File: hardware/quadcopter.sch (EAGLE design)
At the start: 62 parts, among them J1 AVR_SPI_PRG_6NS, J2 HEADER-4POS-2X2-0.1IN-FEMALE-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, J3 HEADER-10POSTH-254X10, J4 HEADER-4POS-0.1IN-FEMALE-SMD-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, Q1 MOSFET-SI2302CDS-T1-E3CT-ND, Q2 MOSFET-SI2302CDS-T1-E3CT-ND, Q3 MOSFET-SI2302CDS-T1-E3CT-ND, Q4 MOSFET-SI2302CDS-T1-E3CT-ND, Q5 MOSFET-SI2302CDS-T1-E3CT-ND, Q6 MOSFET-SI2302CDS-T1-E3CT-ND, SW1 PUSHBUTTON_SMD-VERTICAL-1, U1 ATMEGA128RFA1, U2 LSM-IMU-497-18367-1-NDIMU, Y1 CRYSTAL5X3

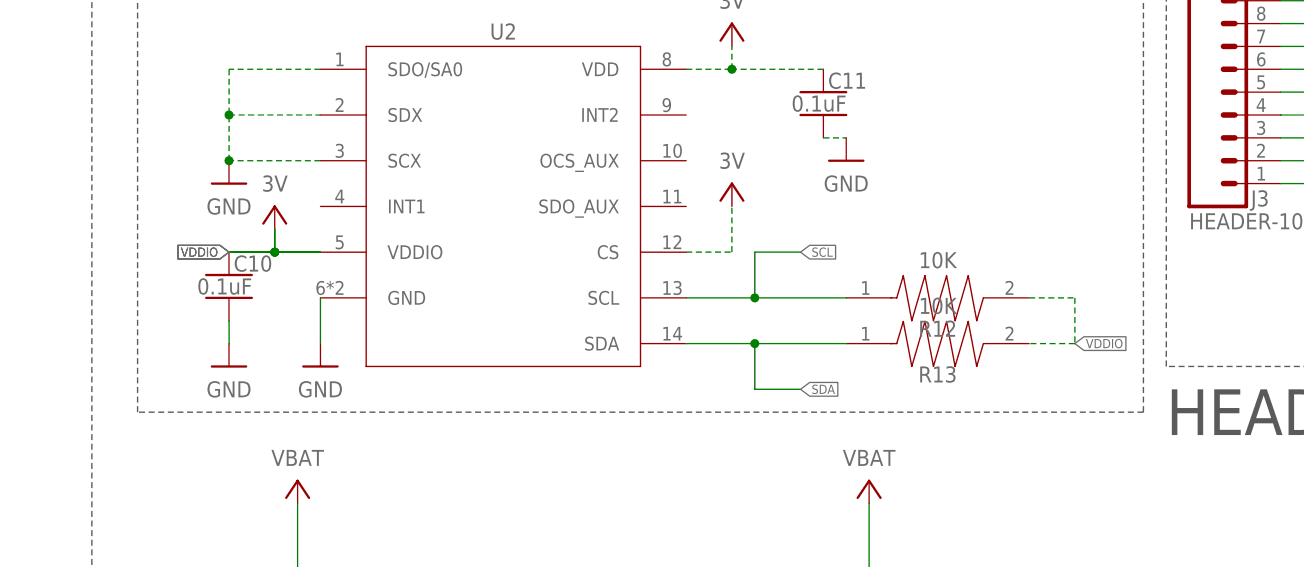
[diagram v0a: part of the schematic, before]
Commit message: switched pull up on SCL and SDA from 'VDDIO' to 3V
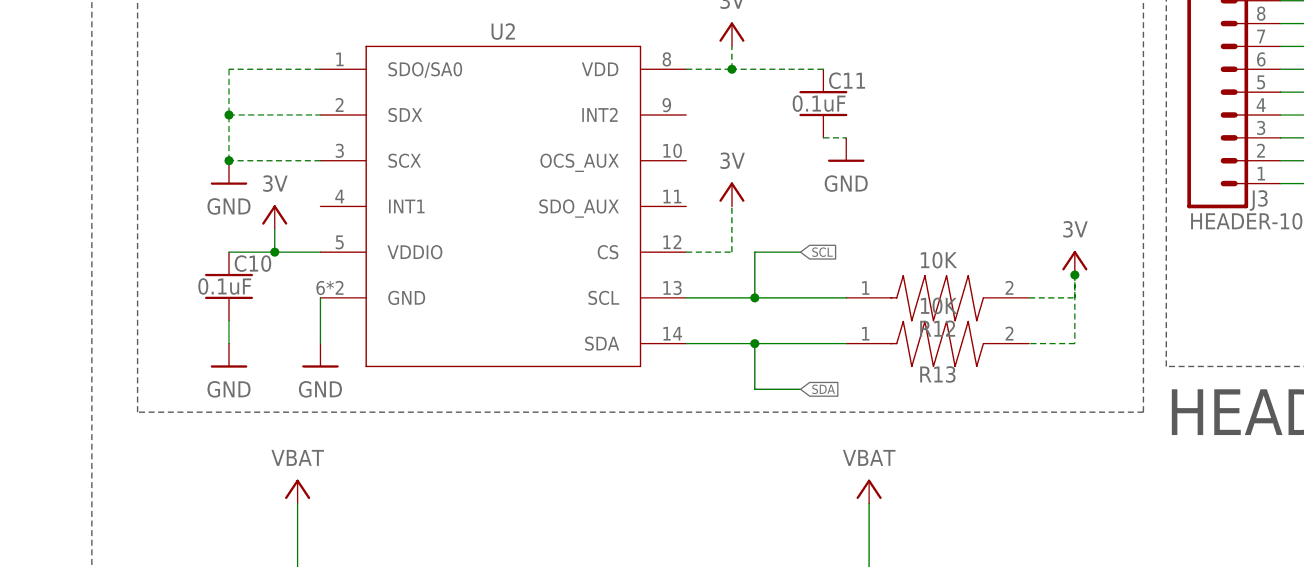
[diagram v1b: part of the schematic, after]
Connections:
- net 3V: now also R12.2, R13.2
- net VDDIO: no longer R12.2, R13.2
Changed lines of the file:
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@@
 <part name="GND4" library="quadparts_prebuilt_2022" deviceset="GND" device=""/>
 <part name="B2" library="quadparts_prebuilt_2022" deviceset="BATTERY" device="-SCREW-TERMINAL"/>
+<part name="P+21" library="quadparts_prebuilt_2022" deviceset="3V" device=""/>
 </parts>
 <sheets>
@@
 <attribute name="NAME" x="242.57" y="45.72" size="1.778" layer="95" font="vector" align="center"/>
 </instance>
+<instance part="P+21" gate="G$1" x="325.12" y="152.4" smashed="yes">
+<attribute name="VALUE" x="325.12" y="154.94" size="1.778" layer="96" rot="R180" align="center"/>
+</instance>
 </instances>
 <busses>
@@
 <pinref part="J3" gate="G$1" pin="10"/>
 </segment>
+<segment>
+<wire x1="320.04" y1="147.32" x2="325.12" y2="147.32" width="0.1524" layer="91" style="longdash"/>
+<wire x1="325.12" y1="147.32" x2="325.12" y2="149.86" width="0.1524" layer="91" style="longdash"/>
+<wire x1="325.12" y1="149.86" x2="325.12" y2="142.24" width="0.1524" layer="91" style="longdash"/>
+<wire x1="325.12" y1="142.24" x2="320.04" y2="142.24" width="0.1524" layer="91" style="longdash"/>
+<pinref part="R12" gate="G$1" pin="2"/>
+<pinref part="R13" gate="G$1" pin="2"/>
+<pinref part="P+21" gate="G$1" pin="3V"/>
+<junction x="325.12" y="149.86"/>
+</segment>
 </net>
 <net name="SCK" class="0">
@@
 <junction x="236.22" y="152.4"/>
 <pinref part="C10" gate="G$1" pin="1"/>
-<label x="231.14" y="152.4" size="1.016" layer="95" rot="R180" xref="yes"/>
-</segment>
-<segment>
-<wire x1="320.04" y1="147.32" x2="325.12" y2="147.32" width="0.1524" layer="91" style="longdash"/>
-<wire x1="325.12" y1="147.32" x2="325.12" y2="142.24" width="0.1524" layer="91" style="longdash"/>
-<wire x1="325.12" y1="142.24" x2="320.04" y2="142.24" width="0.1524" layer="91" style="longdash"/>
-<label x="325.12" y="142.24" size="1.016" layer="95" xref="yes"/>
-<pinref part="R12" gate="G$1" pin="2"/>
-<pinref part="R13" gate="G$1" pin="2"/>
-</segment>
-<segment>
-<pinref part="U2" gate="G$1" pin="VDDIO"/>
-<wire x1="241.3" y1="152.4" x2="236.22" y2="152.4" width="0.1524" layer="91"/>
-<wire x1="236.22" y1="152.4" x2="236.22" y2="154.94" width="0.1524" layer="91"/>
-<pinref part="P+5" gate="G$1" pin="3V"/>
-<wire x1="236.22" y1="152.4" x2="231.14" y2="152.4" width="0.1524" layer="91"/>
-<junction x="236.22" y="152.4"/>
-<pinref part="C10" gate="G$1" pin="1"/>
-<label x="231.14" y="152.4" size="1.016" layer="95" rot="R180" xref="yes"/>
-</segment>
-</net>
+</segment>
+</net>

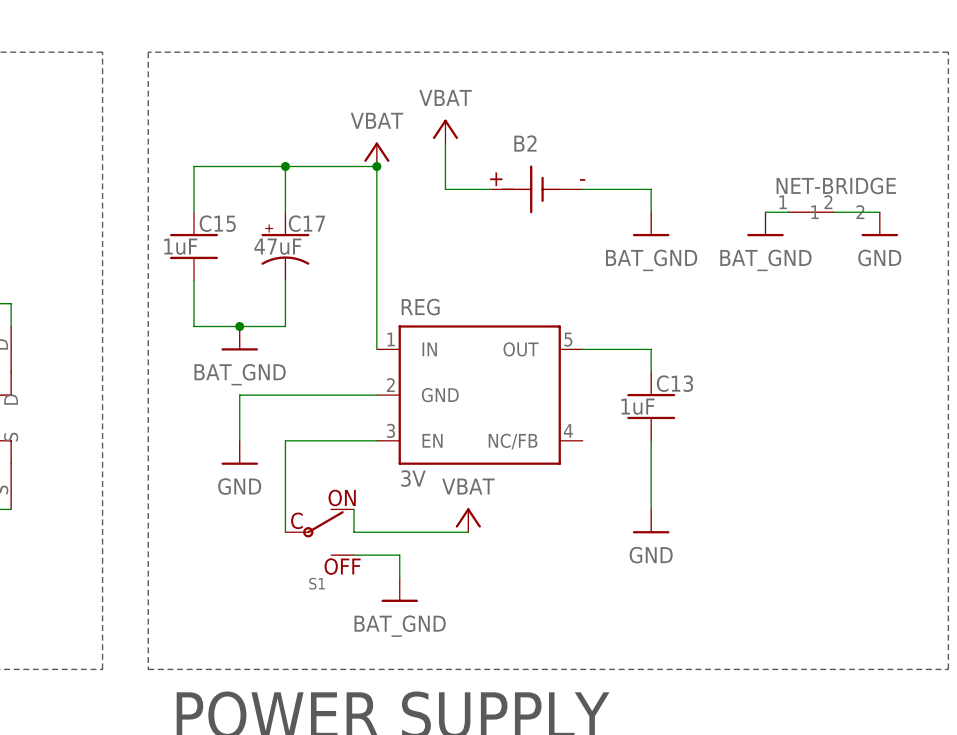
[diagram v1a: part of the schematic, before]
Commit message: moved polarized capacitor by Regulator to regulated side and made out the 3V
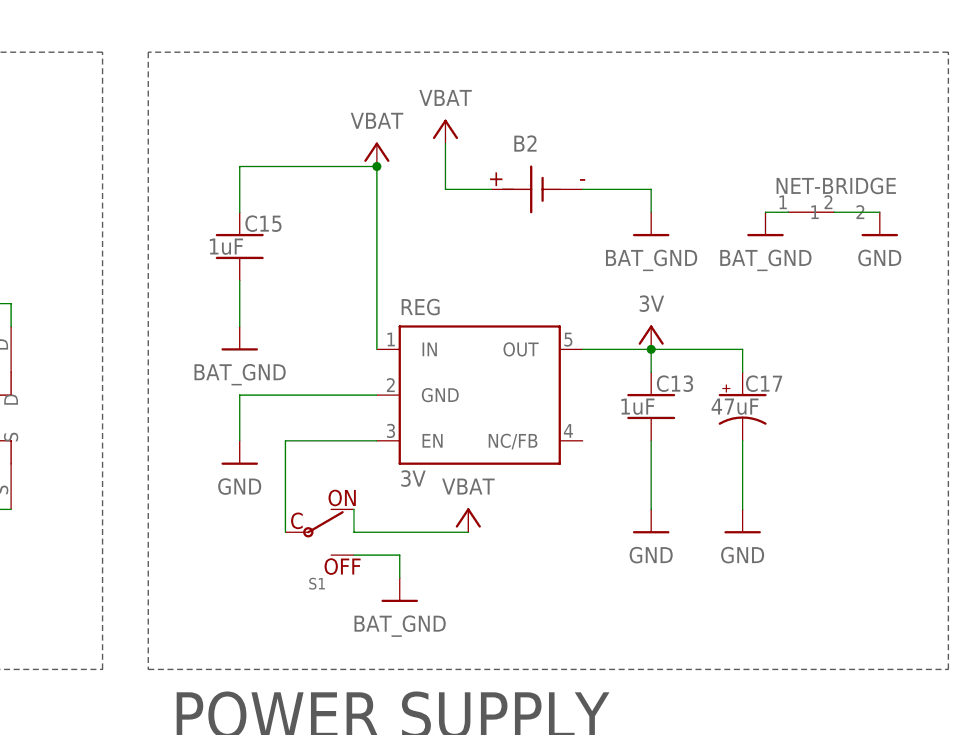
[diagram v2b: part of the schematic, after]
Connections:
- removed net N$18: C13.1, REG.OUT
- net 3V: now also C13.1, C17.+, REG.OUT
- net BAT_GND: no longer C17.-
- net GND: now also C17.-
- net VBAT: no longer C17.+
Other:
- moved on the sheet: C15, C17
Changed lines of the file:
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@@
 <part name="C15" library="quadparts_prebuilt_2022" deviceset="CAPACITOR-NP_" device="SMD-2012-0805_CERAMIC-1UF" value="1uF"/>
 <part name="C13" library="quadparts_prebuilt_2022" deviceset="CAPACITOR-NP_" device="SMD-2012-0805_CERAMIC-1UF" value="1uF"/>
-<part name="C17" library="quadparts_prebuilt_2022" deviceset="CAPACITOR-POL_" device="47UF-SMD-1206-TAJA" package3d_urn="urn:adsk.eagle:package:11793387/1" value="47uF"/>
 <part name="P+5" library="quadparts_prebuilt_2022" deviceset="3V" device=""/>
 <part name="C10" library="quadparts_prebuilt_2022" deviceset="CAPACITOR-NP_" device="SMD-2012-0805_CERAMIC-0.1UF" value="0.1uF"/>
@@
 <part name="B2" library="quadparts_prebuilt_2022" deviceset="BATTERY" device="-SCREW-TERMINAL"/>
 <part name="P+21" library="quadparts_prebuilt_2022" deviceset="3V" device=""/>
+<part name="C17" library="quadparts_prebuilt_2022" deviceset="CAPACITOR-POL_" device="47UF-SMD-1206-TAJA" package3d_urn="urn:adsk.eagle:package:11793387/1" value="47uF"/>
+<part name="GND47" library="quadparts_prebuilt_2022" deviceset="GND" device=""/>
+<part name="P+22" library="quadparts_prebuilt_2022" deviceset="3V" device=""/>
 </parts>
 <sheets>
@@
 <attribute name="NAME" x="297.688" y="170.561" size="1.778" layer="95"/>
 </instance>
-<instance part="C15" gate="G$1" x="205.74" y="35.56" smashed="yes">
-<attribute name="VALUE" x="202.184" y="33.401" size="1.778" layer="96"/>
-<attribute name="NAME" x="206.248" y="35.941" size="1.778" layer="95"/>
+<instance part="C15" gate="G$1" x="210.82" y="35.56" smashed="yes">
+<attribute name="VALUE" x="207.264" y="33.401" size="1.778" layer="96"/>
+<attribute name="NAME" x="211.328" y="35.941" size="1.778" layer="95"/>
 </instance>
 <instance part="C13" gate="G$1" x="256.54" y="17.78" smashed="yes">
@@
 <attribute name="NAME" x="257.048" y="18.161" size="1.778" layer="95"/>
 </instance>
-<instance part="C17" gate="G$1" x="215.9" y="35.56" smashed="yes">
-<attribute name="VALUE" x="212.344" y="33.401" size="1.778" layer="96"/>
-<attribute name="NAME" x="216.154" y="35.941" size="1.778" layer="95"/>
-</instance>
 <instance part="P+5" gate="G$1" x="236.22" y="157.48" smashed="yes">
 <attribute name="VALUE" x="236.22" y="160.02" size="1.778" layer="96" rot="R180" align="center"/>
@@
 <instance part="P+21" gate="G$1" x="325.12" y="152.4" smashed="yes">
 <attribute name="VALUE" x="325.12" y="154.94" size="1.778" layer="96" rot="R180" align="center"/>
+</instance>
+<instance part="C17" gate="G$1" x="266.7" y="17.78" smashed="yes">
+<attribute name="VALUE" x="263.144" y="15.621" size="1.778" layer="96"/>
+<attribute name="NAME" x="266.954" y="18.161" size="1.778" layer="95"/>
+</instance>
+<instance part="GND47" gate="1" x="266.7" y="2.54" smashed="yes">
+<attribute name="VALUE" x="266.7" y="0" size="1.778" layer="96" align="center"/>
+</instance>
+<instance part="P+22" gate="G$1" x="256.54" y="25.4" smashed="yes">
+<attribute name="VALUE" x="256.54" y="27.94" size="1.778" layer="96" rot="R180" align="center"/>
 </instance>
 </instances>
@@
 <label x="86.36" y="119.38" size="1.016" layer="95" xref="yes"/>
 </segment>
+<segment>
+<pinref part="C17" gate="G$1" pin="-"/>
+<wire x1="266.7" y1="12.7" x2="266.7" y2="5.08" width="0.1524" layer="91"/>
+<pinref part="GND47" gate="1" pin="GND"/>
+</segment>
 </net>
 <net name="PG1" class="0">
@@
 <pinref part="P+21" gate="G$1" pin="3V"/>
 <junction x="325.12" y="149.86"/>
+</segment>
+<segment>
+<pinref part="REG" gate="G$1" pin="OUT"/>
+<wire x1="248.92" y1="22.86" x2="256.54" y2="22.86" width="0.1524" layer="91"/>
+<wire x1="256.54" y1="22.86" x2="256.54" y2="20.32" width="0.1524" layer="91"/>
+<pinref part="C13" gate="G$1" pin="1"/>
+<pinref part="C17" gate="G$1" pin="+"/>
+<wire x1="266.7" y1="20.32" x2="266.7" y2="22.86" width="0.1524" layer="91"/>
+<wire x1="266.7" y1="22.86" x2="256.54" y2="22.86" width="0.1524" layer="91"/>
+<junction x="256.54" y="22.86"/>
+<pinref part="P+22" gate="G$1" pin="3V"/>
 </segment>
 </net>
@@
 <pinref part="REG" gate="G$1" pin="IN"/>
 <wire x1="226.06" y1="22.86" x2="226.06" y2="43.18" width="0.1524" layer="91"/>
-<wire x1="226.06" y1="43.18" x2="215.9" y2="43.18" width="0.1524" layer="91"/>
-<wire x1="215.9" y1="43.18" x2="205.74" y2="43.18" width="0.1524" layer="91"/>
-<wire x1="205.74" y1="43.18" x2="205.74" y2="38.1" width="0.1524" layer="91"/>
-<wire x1="215.9" y1="38.1" x2="215.9" y2="43.18" width="0.1524" layer="91"/>
+<wire x1="226.06" y1="43.18" x2="210.82" y2="43.18" width="0.1524" layer="91"/>
+<wire x1="210.82" y1="43.18" x2="210.82" y2="38.1" width="0.1524" layer="91"/>
+<pinref part="C15" gate="G$1" pin="1"/>
 <junction x="226.06" y="43.18"/>
-<junction x="215.9" y="43.18"/>
-<pinref part="C15" gate="G$1" pin="1"/>
-<pinref part="C17" gate="G$1" pin="+"/>
 </segment>
 <segment>
@@
 </segment>
 <segment>
-<wire x1="205.74" y1="30.48" x2="205.74" y2="25.4" width="0.1524" layer="91"/>
-<wire x1="215.9" y1="30.48" x2="215.9" y2="25.4" width="0.1524" layer="91"/>
-<wire x1="215.9" y1="25.4" x2="210.82" y2="25.4" width="0.1524" layer="91"/>
+<wire x1="210.82" y1="30.48" x2="210.82" y2="25.4" width="0.1524" layer="91"/>
 <pinref part="GND33" gate="1" pin="BAT_GND"/>
-<wire x1="210.82" y1="25.4" x2="205.74" y2="25.4" width="0.1524" layer="91"/>
-<junction x="210.82" y="25.4"/>
 <pinref part="C15" gate="G$1" pin="2"/>
-<pinref part="C17" gate="G$1" pin="-"/>
 </segment>
 </net>
@@
 </segment>
 </net>
-<net name="N$18" class="0">
-<segment>
-<pinref part="REG" gate="G$1" pin="OUT"/>
-<wire x1="248.92" y1="22.86" x2="256.54" y2="22.86" width="0.1524" layer="91"/>
-<wire x1="256.54" y1="22.86" x2="256.54" y2="20.32" width="0.1524" layer="91"/>
-<pinref part="C13" gate="G$1" pin="1"/>
-</segment>
-</net>

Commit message: redid VDDIO
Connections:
- removed net VDDIO: C10.1, U2.VDDIO
- net 3V: now also C10.1, U2.VDDIO
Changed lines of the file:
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@@
 <pinref part="P+22" gate="G$1" pin="3V"/>
+</segment>
+<segment>
+<pinref part="U2" gate="G$1" pin="VDDIO"/>
+<wire x1="241.3" y1="152.4" x2="236.22" y2="152.4" width="0.1524" layer="91"/>
+<wire x1="236.22" y1="152.4" x2="236.22" y2="154.94" width="0.1524" layer="91"/>
+<pinref part="P+5" gate="G$1" pin="3V"/>
+<pinref part="C10" gate="G$1" pin="1"/>
+<wire x1="231.14" y1="152.4" x2="236.22" y2="152.4" width="0.1524" layer="91"/>
+<junction x="236.22" y="152.4"/>
 </segment>
 </net>
@@
 </segment>
 </net>
-<net name="VDDIO" class="0">
-<segment>
-<pinref part="U2" gate="G$1" pin="VDDIO"/>
-<wire x1="241.3" y1="152.4" x2="236.22" y2="152.4" width="0.1524" layer="91"/>
-<wire x1="236.22" y1="152.4" x2="236.22" y2="154.94" width="0.1524" layer="91"/>
-<pinref part="P+5" gate="G$1" pin="3V"/>
-<wire x1="236.22" y1="152.4" x2="231.14" y2="152.4" width="0.1524" layer="91"/>
-<junction x="236.22" y="152.4"/>
-<pinref part="C10" gate="G$1" pin="1"/>
-</segment>
-</net>
